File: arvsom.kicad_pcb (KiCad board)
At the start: 12 copper layers, 55 x 40 mm, 413 parts, among them J1 TAG-10PIN, J3 DF40C-100DP-0.4V(51), J4 DF40C-100DP-0.4V(51), Q1 DMG1013UWQ-7, Q5 DMG1012UW, U1 MT53D1024M32D4DT-053, U10 TDA19988BHN_C1,557, U11 KSZ9031RNXCA, U13 VIC7100, U2 GD25LQ256DWIGR, U3 MT53D1024M32D4DT-053, U4 CSD86330Q3D, U5 LMR62014XMF_NOPB, U6 CSD86330Q3D, U7 STM811RW16F, U8 TPS65086100, Y1 ABM8G-25.000MHZ-18-D2Y-T, Y2 ABM8G-25.000MHZ-18-D2Y-T, Y3 ABM8G-27.000MHZ-18-D2Y-T

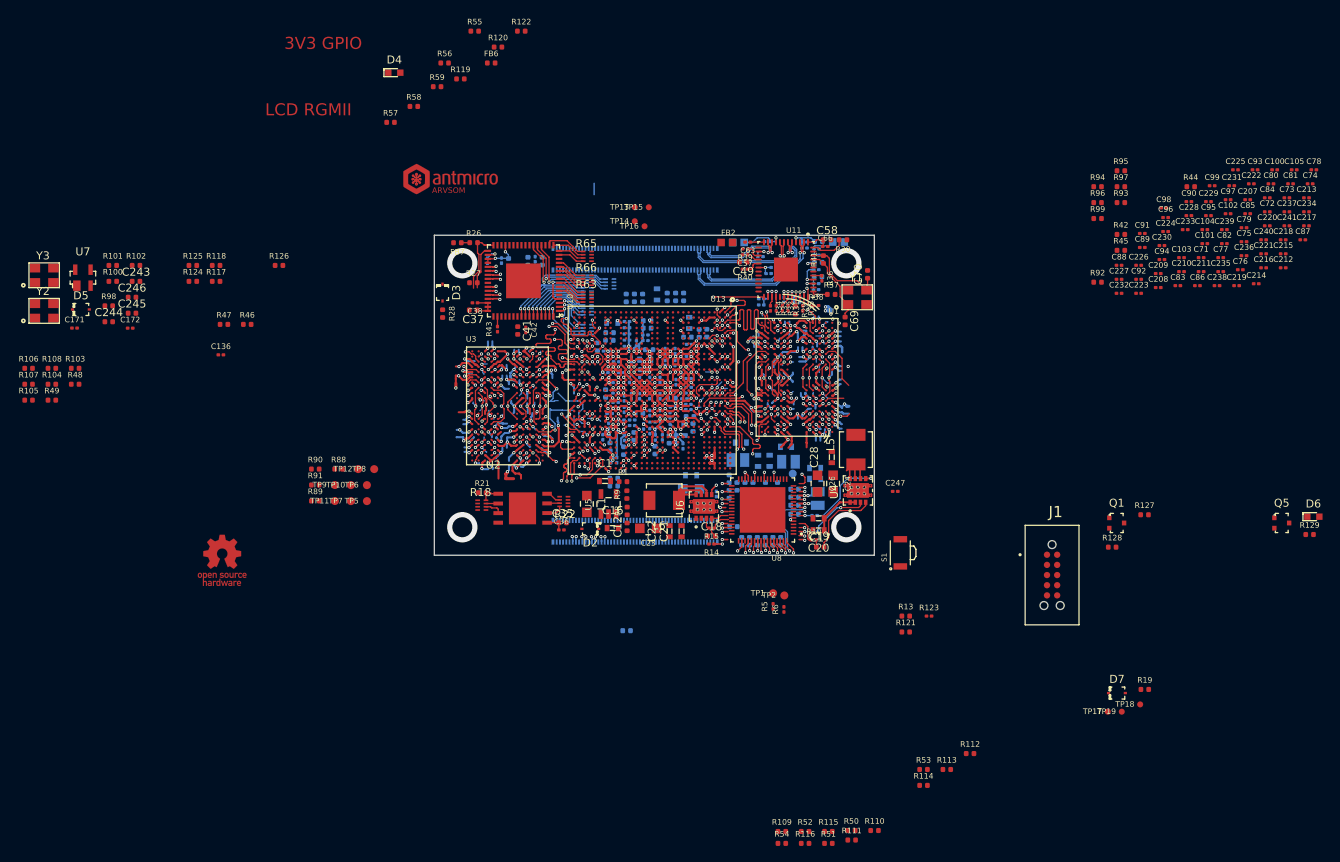
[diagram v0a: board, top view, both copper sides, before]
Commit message: Updated component placement - DDR decoupling done
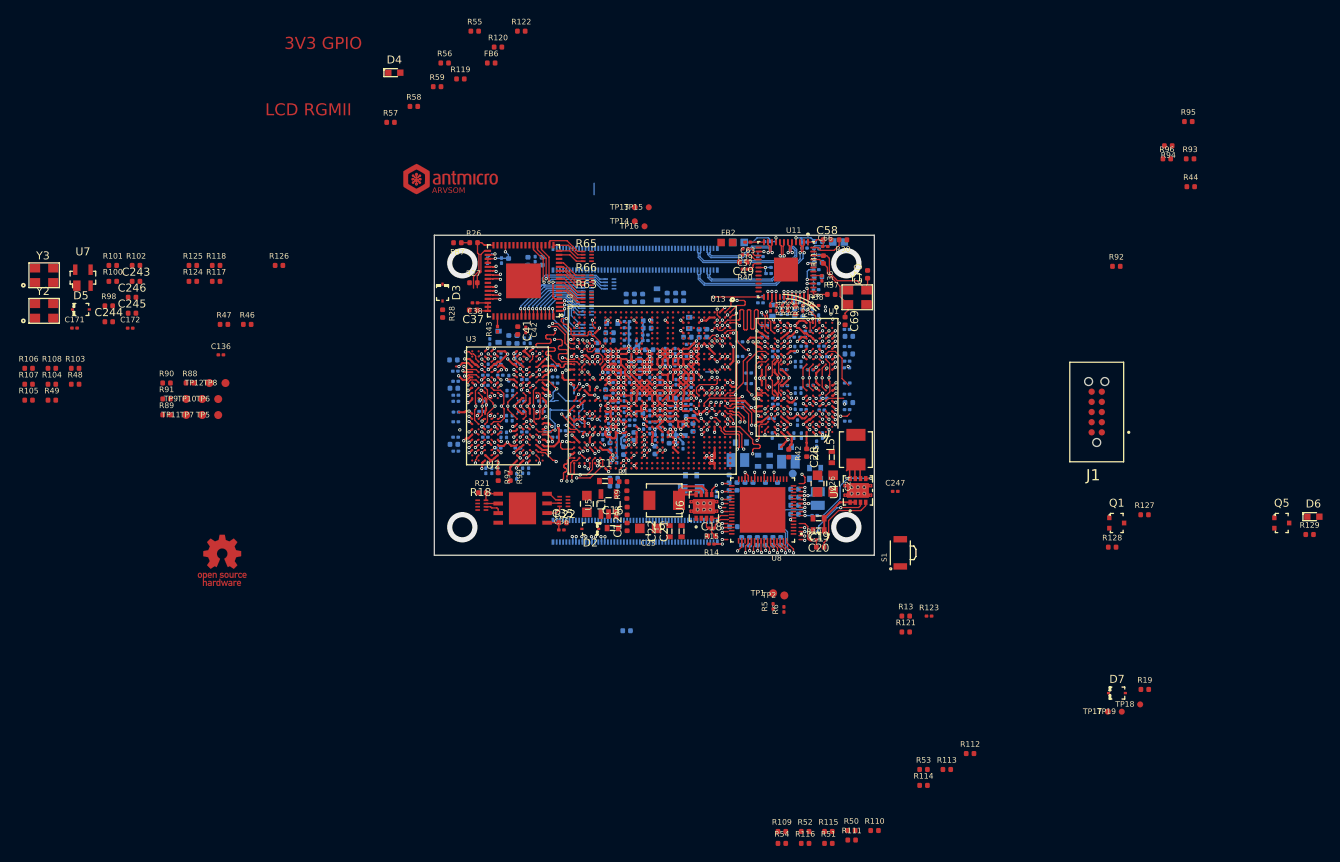
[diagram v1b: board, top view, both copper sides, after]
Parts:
- added C247: C_100n_0201, arvsom-footprints:0201-res, B.Cu at (168.2, 76.5)
- added C248: C_100n_0201, arvsom-footprints:0201-res, B.Cu at (171.3, 67.7)
- added C249: C_10u_0402, arvsom-footprints:0402-cap, B.Cu at (181.8, 69.8)
- added C250: C_100n_0201, arvsom-footprints:0201-res, B.Cu at (178.4, 68.8)
- added C251: C_10u_0402, arvsom-footprints:0402-cap, B.Cu at (181.8, 75.9)
- added C252: C_10u_0402, arvsom-footprints:0402-cap, B.Cu at (176.1, 64.7)
- added C253: C_10u_0402, arvsom-footprints:0402-cap, B.Cu at (181.8, 67.6)
- added C254: C_1u_0402, arvsom-footprints:0402-cap, B.Cu at (175.1, 64.7)
- added C255: C_22u_0603, arvsom-footprints:0603-cap, B.Cu at (172.3, 64.4)
- added C256: C_1u_0402, arvsom-footprints:0402-cap, B.Cu at (140.4, 68.0)
- added C257: C_22u_0603, arvsom-footprints:0603-cap, B.Cu at (138.1, 67.7)
- added C258: C_10u_0402, arvsom-footprints:0402-cap, B.Cu at (139.3, 68.0)
- added C259: C_10u_0402, arvsom-footprints:0402-cap, B.Cu at (132.4, 70.6)
- added C260: C_10u_0402, arvsom-footprints:0402-cap, B.Cu at (132.5, 81.1)
- added C261: C_100n_0201, arvsom-footprints:0201-res, B.Cu at (140.1, 70.0)
- added C262: C_10u_0402, arvsom-footprints:0402-cap, B.Cu at (132.5, 74.1)
- added C263: C_100n_0201, arvsom-footprints:0201-res, B.Cu at (138.0, 71.1)
- added C264: C_100n_0201, arvsom-footprints:0201-res, B.Cu at (136.4, 73.7)
- added C265: C_100n_0201, arvsom-footprints:0201-res, B.Cu at (178.7, 70.2)
- added C266: C_100n_0201, arvsom-footprints:0201-res, B.Cu at (178.7, 75.3)
- added C267: C_100n_0201, arvsom-footprints:0201-res, B.Cu at (145.1, 72.7)
- added C268: C_100n_0201, arvsom-footprints:0201-res, B.Cu at (141.3, 73.0)
- added C269: C_100n_0201, arvsom-footprints:0201-res, B.Cu at (175.9, 80.0)
- added C270: C_100n_0201, arvsom-footprints:0201-res, B.Cu at (181.6, 78.2)
- added C271: C_100n_0201, arvsom-footprints:0201-res, B.Cu at (178.5, 80.0)
- added C272: C_100n_0201, arvsom-footprints:0201-res, B.Cu at (172.6, 76.1)
- added C273: C_100n_0201, arvsom-footprints:0201-res, B.Cu at (172.3, 80.0)
- added C274: C_100n_0201, arvsom-footprints:0201-res, B.Cu at (171.3, 66.3)
- added C275: C_100n_0201, arvsom-footprints:0201-res, B.Cu at (178.1, 65.3)
- added C276: C_100n_0201, arvsom-footprints:0201-res, B.Cu at (174.2, 64.5)
- added C277: C_100n_0201, arvsom-footprints:0201-res, B.Cu at (172.6, 69.4)
- added C278: C_100n_0201, arvsom-footprints:0201-res, B.Cu at (176.7, 67.0)
- added C279: C_100n_0201, arvsom-footprints:0201-res, B.Cu at (138.0, 84.4)
- added C280: C_100n_0201, arvsom-footprints:0201-res, B.Cu at (141.8, 84.4)
- added C281: C_100n_0201, arvsom-footprints:0201-res, B.Cu at (132.7, 72.0)
- added C282: C_100n_0201, arvsom-footprints:0201-res, B.Cu at (140.5, 71.1)
- added C283: C_100n_0201, arvsom-footprints:0201-res, B.Cu at (136.5, 84.4)
- added C284: C_100n_0201, arvsom-footprints:0201-res, B.Cu at (136.4, 78.9)
- added C285: C_100n_0201, arvsom-footprints:0201-res, B.Cu at (138.0, 81.6)
- added C286: C_100n_0201, arvsom-footprints:0201-res, B.Cu at (132.7, 82.0)
- added C287: C_100n_0201, arvsom-footprints:0201-res, B.Cu at (136.4, 72.5)
- added C288: C_100n_0201, arvsom-footprints:0201-res, B.Cu at (145.1, 71.2)
- C100, C101, C102, C103, C104, C105, C207, C208, C209, C210, C211, C212, C213, C214, C215, C216, C217, C218, C219, C220, C221, C222, C223, C224, C225, C226, C227, C228, C229, C230, C231, C232, C233, C234, C235, C236, C237, C238, C239, C240, C241, C71, C72, C73, C74, C75, C76, C77, C78, C79, C80, C81, C82, C83, C84, C85, C86, C87, C88, C89, C90, C91, C92, C93, C94, C95, C96, C97, C98, C99: moved to B.Cu
- moved C218 106.3 mm to (132.7, 80.2), turned to 180 degrees
- moved C217 103.8 mm to (136.8, 71.4), turned to 270 degrees
- moved C213 103.8 mm to (141.1, 84.4), turned to 270 degrees
- moved C207 102.8 mm to (132.7, 78.3), turned to 180 degrees
- moved C225 101.7 mm to (132.7, 75.7), turned to 180 degrees
- moved C231 101.0 mm to (132.7, 77.1), turned to 180 degrees
- moved C220 100.6 mm to (136.0, 75.7), turned to 180 degrees
- moved C240 100.1 mm to (135.9, 77.0), turned to 180 degrees
- moved C234 98.8 mm to (144.2, 79.5), turned to 180 degrees
- moved C221 98.0 mm to (138.3, 79.9), turned to 270 degrees
- moved C216 96.9 mm to (139.0, 79.9), turned to 90 degrees
- moved C235 96.9 mm to (132.7, 75.0), turned to 180 degrees
- moved C222 96.2 mm to (138.4, 70.0), turned to 270 degrees
- moved C237 95.9 mm to (142.0, 68.2), turned to 90 degrees
- moved C238 95.9 mm to (132.7, 73.2), turned to 180 degrees
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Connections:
- C225 pad 1: Net-(C225-Pad1) -> VCC_1V1
- C230 pad 1: Net-(C230-Pad1) -> VCC_1V1
- U3 pad F1: VCC_1V8 -> VDD1_1V8
- U3 pad F12: VCC_1V8 -> VDD1_1V8
- U3 pad G4: VCC_1V8 -> VDD1_1V8
- U3 pad G9: VCC_1V8 -> VDD1_1V8
- U3 pad T4: VCC_1V8 -> VDD1_1V8
- U3 pad T9: VCC_1V8 -> VDD1_1V8
- U3 pad U1: VCC_1V8 -> VDD1_1V8
- U3 pad U12: VCC_1V8 -> VDD1_1V8
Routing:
- net GND: track 339.4 -> 274.7 mm
- net VCC_1V1: track 158.9 -> 129.3 mm, vias 105 -> 104
- net VCC_1V8: track 62.6 -> 39.9 mm, vias 28 -> 19
- net VDD1_1V8: track 0.00 -> 8.97 mm, vias 0 -> 8
- net (no net): track 15.6 -> 11.5 mm
- net VDDQ: track 2.15 -> 0.00 mm
- net DDR0_CS3: track 26.9 -> 25.4 mm
- net Net-(R99-Pad1): track 3.24 -> 1.90 mm
- net VCC_1V2: track 11.8 -> 10.5 mm
- net DDR0_A00: track 24.5 -> 23.2 mm
- net DDR0_CS1: track 23.8 -> 22.5 mm
- net DDR0_A01: track 23.3 -> 22.0 mm
- net DDR0_DQ00: track 23.1 -> 21.9 mm
- net DDR0_CS0: track 27.8 -> 26.6 mm
- net DDR0_DQ16: track 21.5 -> 20.5 mm
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
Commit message: Finished component placement
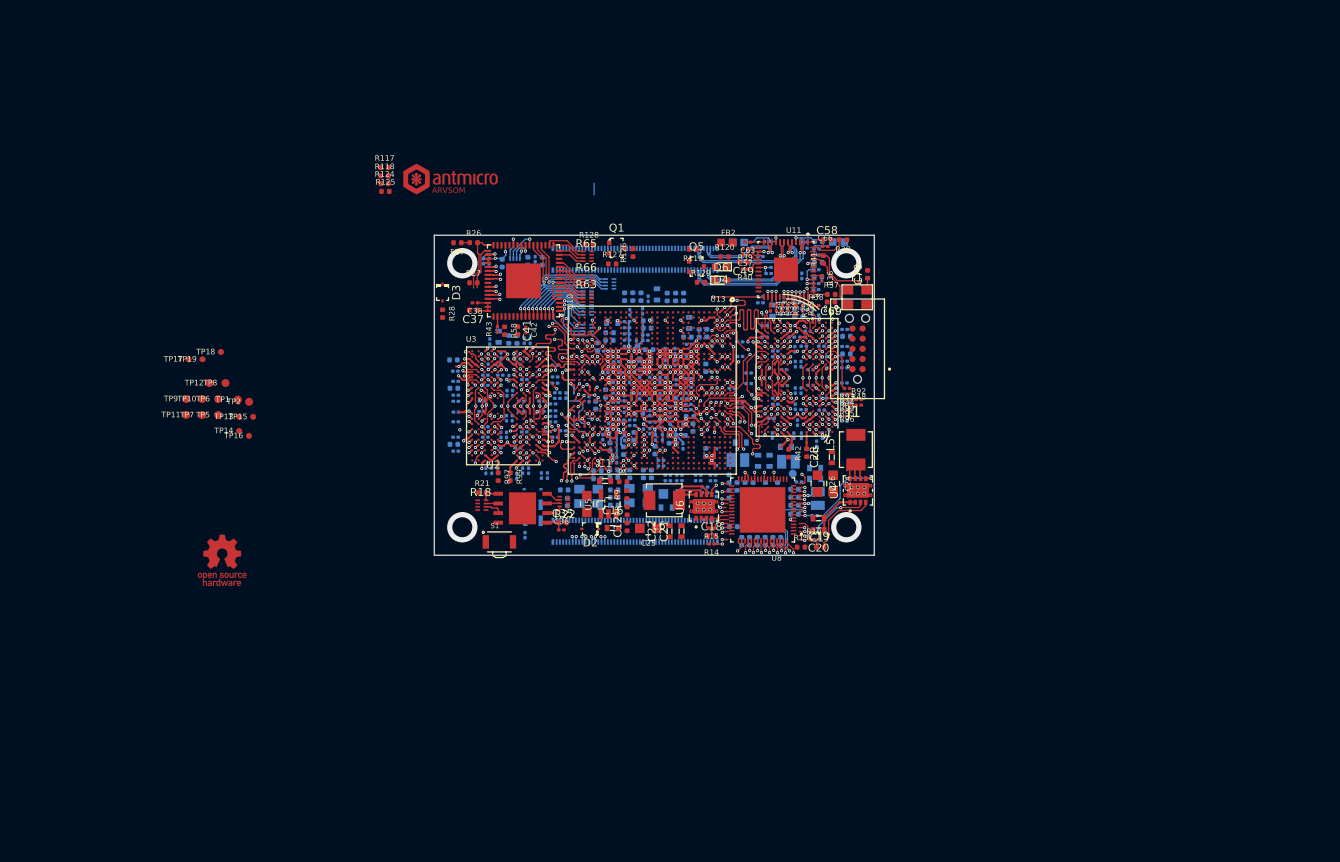
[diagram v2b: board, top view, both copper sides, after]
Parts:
- removed the C247 at (187.6, 87.0)
- removed R55, R56, R57, R59: R_33R_0402, arvsom-footprints:0402-res
- added R20: 4x33R_0201_array, arvsom-footprints:EXB18V, B.Cu at (140.1, 58.4)
- C136, C171, C172, C243, C244, C245, C246, D5, D7, FB6, R100, R101, R102, R121, R123, R19, R5, R6, R89, R91, R98, U7, Y2, Y3: moved to B.Cu
- R103, R104, R105, R106, R107, R108, R109, R110, R111, R112, R113, R114, R115, R116, R122, R49, R50, R51, R52, R53, R54, R88, R90: value R_10k_0402 -> R_10k_0201; footprint arvsom-footprints:0402-res -> arvsom-footprints:0201-res; moved to B.Cu
- R44, R92, R93, R94, R95, R96: value R_10k_0402 -> R_10k_0201; footprint arvsom-footprints:0402-res -> arvsom-footprints:0201-res
- R46, R47: value R_0R_0402 -> R_0R_0201; footprint arvsom-footprints:0402-res -> arvsom-footprints:0201-res; moved to B.Cu
- R48: value R_0R_0402 -> R_0R_0201; footprint arvsom-footprints:0402-res -> arvsom-footprints:0201-res
- moved TP18 123.1 mm to (103.3, 69.6)
- moved TP17 123.1 mm to (99.3, 70.5)
- moved TP19 123.1 mm to (101.0, 70.5)
- moved R48 98.0 mm to (183.1, 76.2)
- moved R129 82.3 mm to (163.4, 60.9)
- moved Q5 79.9 mm to (162.8, 58.9)
- moved D6 79.7 mm to (165.9, 60.6)
- moved Y3 79.3 mm to (155.6, 87.5), turned to 180 degrees
- moved R128 75.6 mm to (149.4, 56.1)
- moved R127 73.6 mm to (152.3, 58.6)
- moved R47 72.5 mm to (176.0, 60.1), turned to 90 degrees
- moved Y2 72.0 mm to (149.4, 87.6), turned to 180 degrees
- moved Q1 71.3 mm to (152.8, 56.6)
- moved TP2 71.1 mm to (106.9, 75.8)
- moved TP1 71.1 mm to (105.5, 75.6)
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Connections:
- R48 pad 1: DDR0_ODT_1 -> DDR0_ODT_0
- R48 pad 2: DDR0_ODT_0 -> DDR0_ODT_1
- R53 pad 2: Net-(R53-Pad2) -> GND
- U3 pad F1: VDD1_1V8 -> VCC_1V8
- U3 pad F12: VDD1_1V8 -> VCC_1V8
- U3 pad G4: VDD1_1V8 -> VCC_1V8
- U3 pad G9: VDD1_1V8 -> VCC_1V8
- U3 pad T4: VDD1_1V8 -> VCC_1V8
- U3 pad T9: VDD1_1V8 -> VCC_1V8
- U3 pad U1: VDD1_1V8 -> VCC_1V8
- U3 pad U12: VDD1_1V8 -> VCC_1V8
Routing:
- net VCC_1V8: track 39.9 -> 48.9 mm, vias 19 -> 27
- net VDD1_1V8: track 8.97 -> 0.00 mm, vias 8 -> 0
- net DDR1_ODT0: track 12.3 -> 6.72 mm
- net DDR1_ODT1: track 13.8 -> 9.03 mm
- net HDMI_BCLK: track 0.00 -> 4.38 mm, vias 0 -> 1
- net HDMI_12MHZ: track 0.00 -> 3.37 mm, vias 0 -> 1
- net HDMI_LRCLK: track 0.00 -> 3.20 mm, vias 0 -> 1
- net HDMI_I2S_TX0: track 0.00 -> 1.73 mm, vias 0 -> 1
- net Net-(C69-Pad1): track 9.59 -> 7.86 mm
- net HDMI_1V8: track 8.63 -> 7.88 mm
- net HDMI_SWING: track 2.11 -> 2.70 mm
- net GND: track 274.7 -> 274.3 mm, vias 235 -> 234
- net DDR0_ODT_0: vias 0 -> 1
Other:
- board text removed: "3V3 GPIO"
- board text removed: "LCD RGMII"

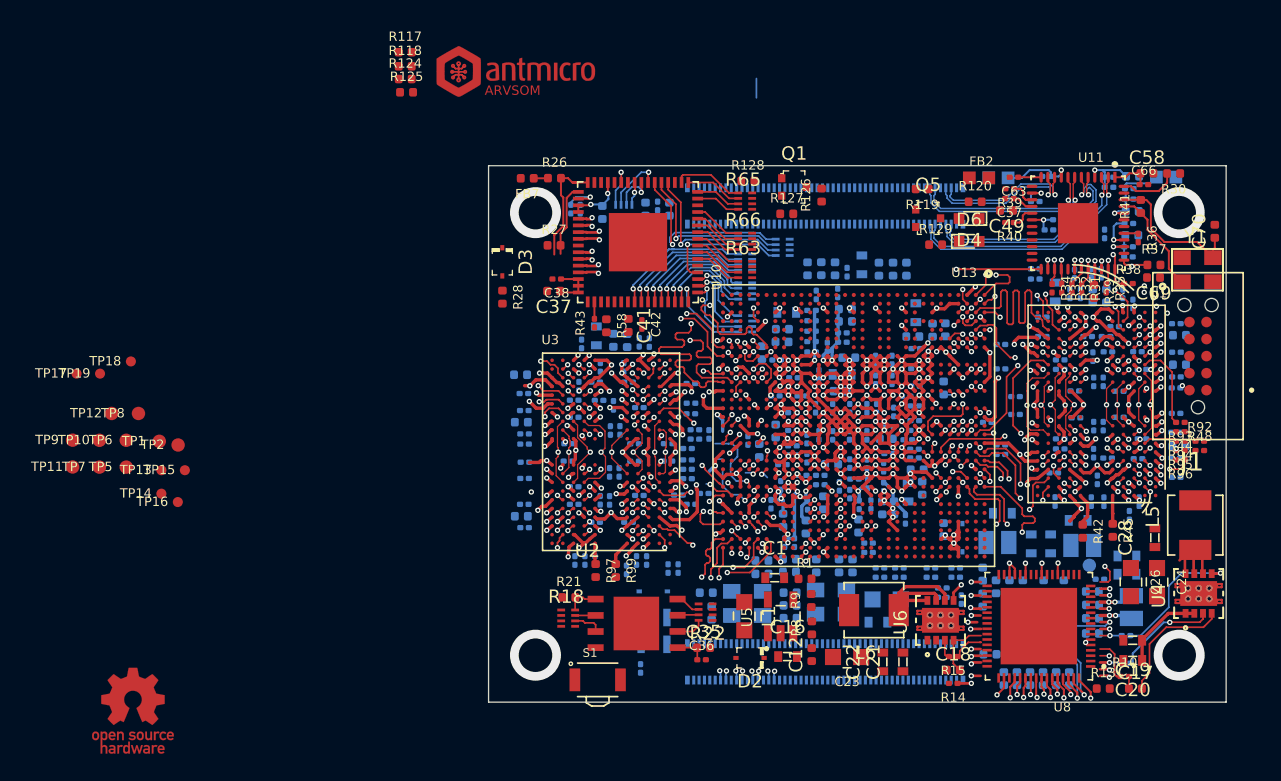
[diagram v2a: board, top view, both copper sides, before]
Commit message: RGMII sketch, started LCD
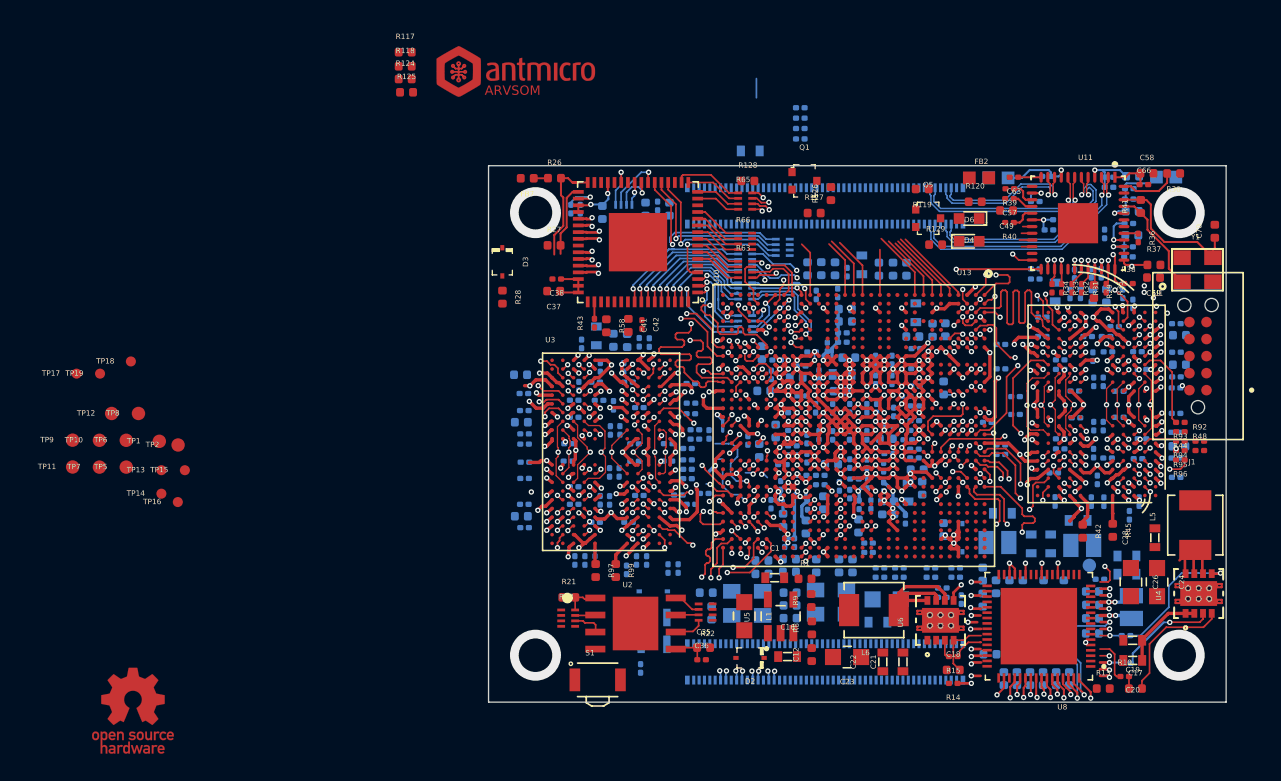
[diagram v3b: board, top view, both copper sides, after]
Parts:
- U2: footprint arvsom-footprints:8-WSON-6x5 -> arvsom-footprints:GD25Q16CWIG
- moved C193 15.1 mm to (153.3, 51.4)
- moved C196 15.1 mm to (153.3, 50.6)
- moved C204 15.1 mm to (153.3, 53.0)
- moved C190 15.1 mm to (153.3, 52.2)
- moved C109 12.3 mm to (149.5, 53.9)
- moved C160 4.80 mm to (150.5, 71.8), turned to 180 degrees
- moved U2 3.92 mm to (141.0, 89.1)
- moved C114 2.86 mm to (153.0, 70.8)
- moved R127 2.05 mm to (154.3, 58.5)
- moved C137 1.59 mm to (151.1, 70.6), turned to 90 degrees
- moved C130 1.05 mm to (153.3, 69.9)
- moved Q1 0.90 mm to (153.6, 56.1)
- moved R126 0.70 mm to (155.6, 57.0)
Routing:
- net RGMII_RXDV: track 2.30 -> 26.5 mm
- net RGMII_TXD0: track 0.46 -> 24.4 mm
- net RGMII_TXEN: track 6.81 -> 29.1 mm
- net RGMII_MDIO: track 2.84 -> 23.3 mm
- net RGMII_RXD2: track 2.35 -> 20.9 mm
- net RGMII_TXD3: track 0.46 -> 18.9 mm
- net RGMII_MDC: track 3.22 -> 21.7 mm
- net RGMII_GTXCLK: track 0.46 -> 18.7 mm, vias 1 -> 2
- net RGMII_RXD0: track 2.42 -> 20.4 mm
- net RGMII_RXD1: track 2.52 -> 20.4 mm
- net RGMII_RXCLK: track 2.29 -> 19.4 mm
- net RGMII_TXD1: track 0.46 -> 17.5 mm
- net RGMII_RXD3: track 2.34 -> 19.3 mm
- net RGMII_TXD2: track 0.46 -> 17.3 mm
- net Net-(R65-Pad7): track 1.75 -> 14.0 mm, vias 1 -> 2
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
